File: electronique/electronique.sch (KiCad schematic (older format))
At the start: 52 parts, among them J1 Conn_01x02, J10 PHOTOD3, J11 PHOTOD4, J12 Ultrason 3, J13 Moteur 2, J14 Moteur 1, J2 Conn_02x07_Odd_Even, J3 Camera, J4 TOF1, J5 Conn_01x06, J6 Ultrason 1, J7 PHOTOD1, J8 PHOTOD2, J9 Ultrason 2, SW1 SW_Push, U1 LD1117S50TR_SOT223, U2 LD1117S33TR_SOT223, U3 STM32L451RETx, U4 LB1930MC-AH, U5 LB1930MC-AH, U6 MAX40056FAUA+, U7 MAX40056FAUA+, Y1 LFXTAL003240

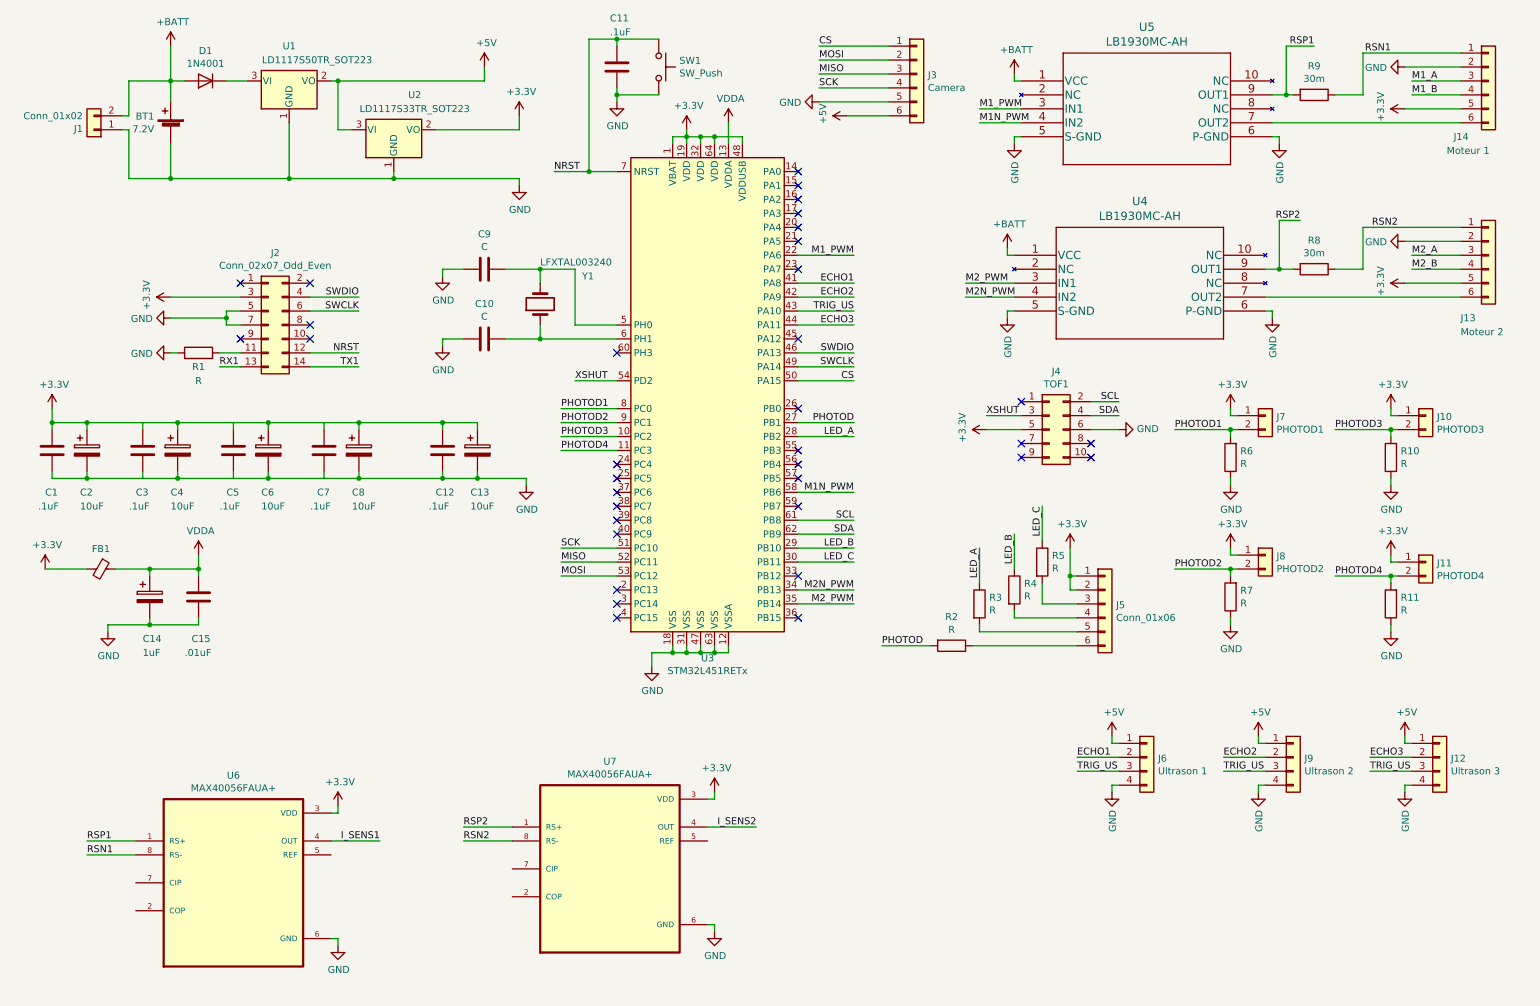
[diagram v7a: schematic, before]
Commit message: Schema de concept termine, il manque les valeurs de certains condensateurs, il est possible qu'il y aie besoin de plus de condensateurs.
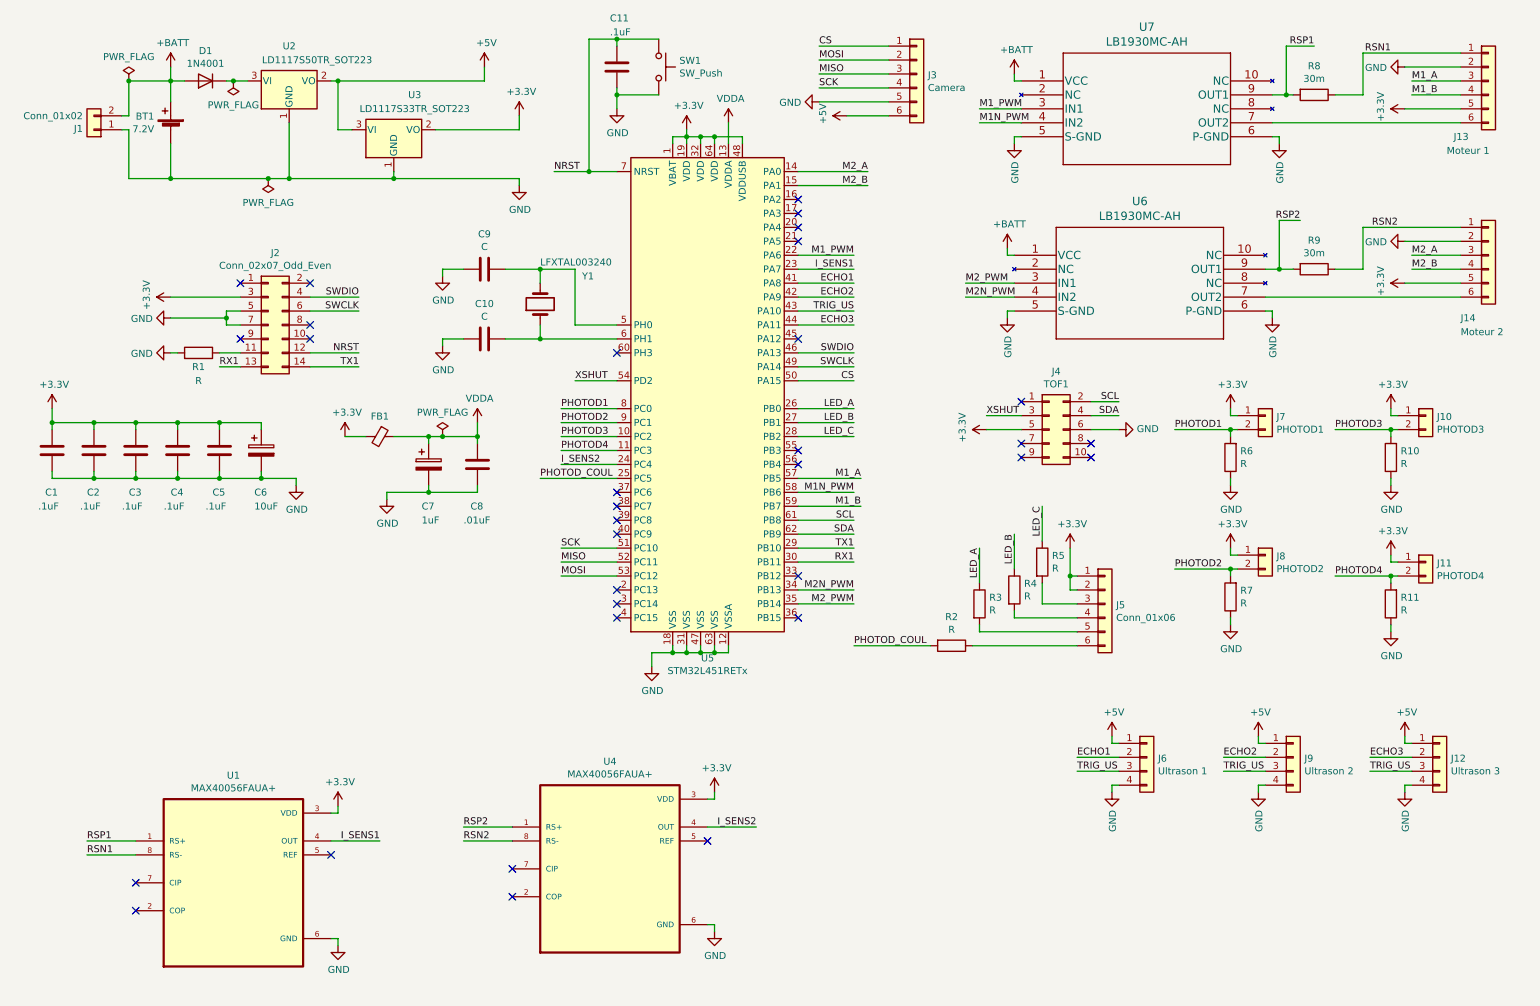
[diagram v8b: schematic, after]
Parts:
- removed C2, C4, C6, C8: 10uF, Capacitor_Tantalum_SMD:CP_EIA-2012-12_Kemet-R_Pad1.30x1.05mm_HandSolder, symbol Device:CP
- C10, C9: footprint Capacitor_SMD:C_0805_2012Metric_Pad1.15x1.40mm_HandSolder -> Capacitor_SMD:C_0805_2012Metric_Pad1.18x1.45mm_HandSolder
- Y1: footprint (none) -> lumos_minima:HC494H
- renumbered C3 to C2, C5 to C3, C7 to C4, C12 to C5, C13 to C6, C14 to C7, C15 to C8, J14 to J13, J13 to J14, R9 to R8, R8 to R9, U6 to U1, U1 to U2, U2 to U3, U7 to U4, U3 to U5, U4 to U6, U5 to U7
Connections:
- net I_SENS1: now also U5.23 (PA7)
- net I_SENS2: now also U5.24 (PC4)
- net LED_A: now also U5.26 (PB0); no longer U5.28 (PB2)
- net LED_B: now also U5.27 (PB1); no longer U5.29 (PB10)
- net LED_C: now also U5.28 (PB2); no longer U5.30 (PB11)
- net M1_A: now also U5.57 (PB5)
- net M1_B: now also U5.59 (PB7)
- net M2_A: now also U5.14 (PA0)
- net M2_B: now also U5.15 (PA1)
- net RX1: now also U5.30 (PB11)
- net TX1: now also U5.29 (PB10)
- net PHOTOD_COUL: now reaches U5.25 (PC5)
- net PHOTOD_COUL: now also R2.2
- removed net PHOTOD: R2.2, U5.27 (PB1)
- no-connect marks 35 -> 33
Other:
- moved on the sheet: C2, C3, C4, C5, C6, C7, C8, FB1
